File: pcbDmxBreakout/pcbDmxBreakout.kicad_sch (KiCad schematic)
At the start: 16 parts

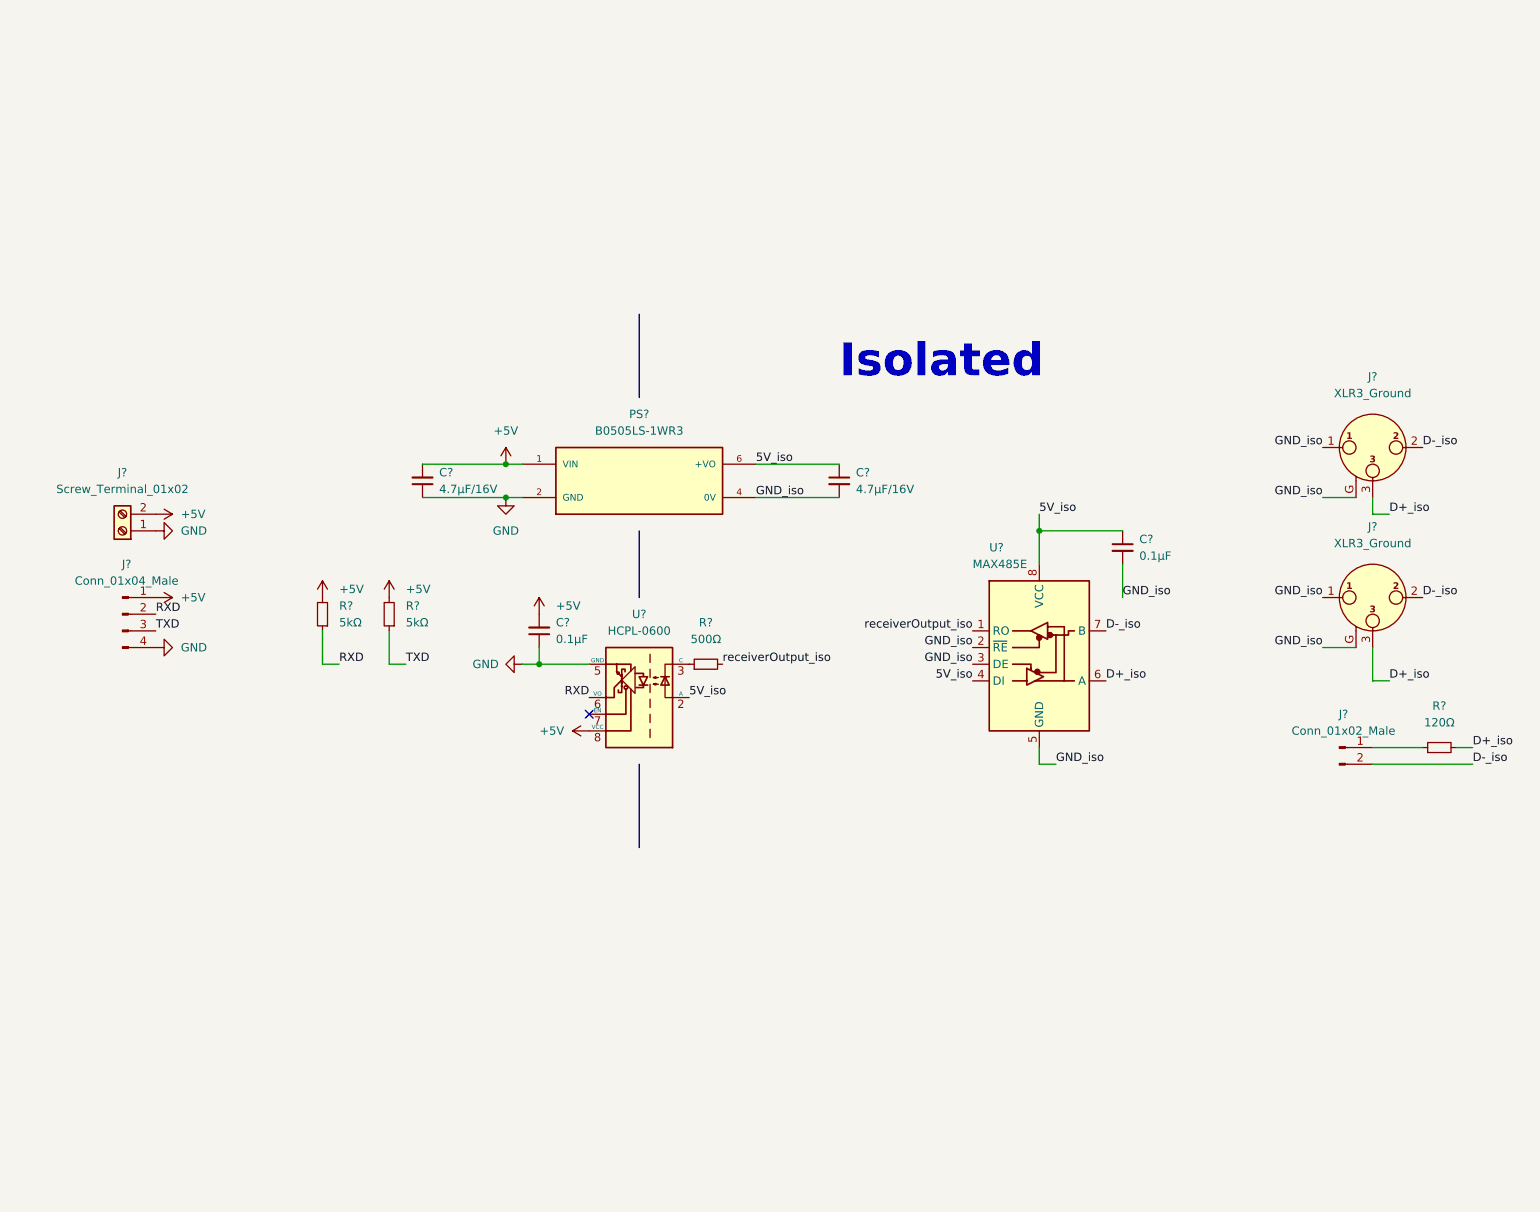
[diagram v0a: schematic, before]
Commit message: add Breakout board PCB
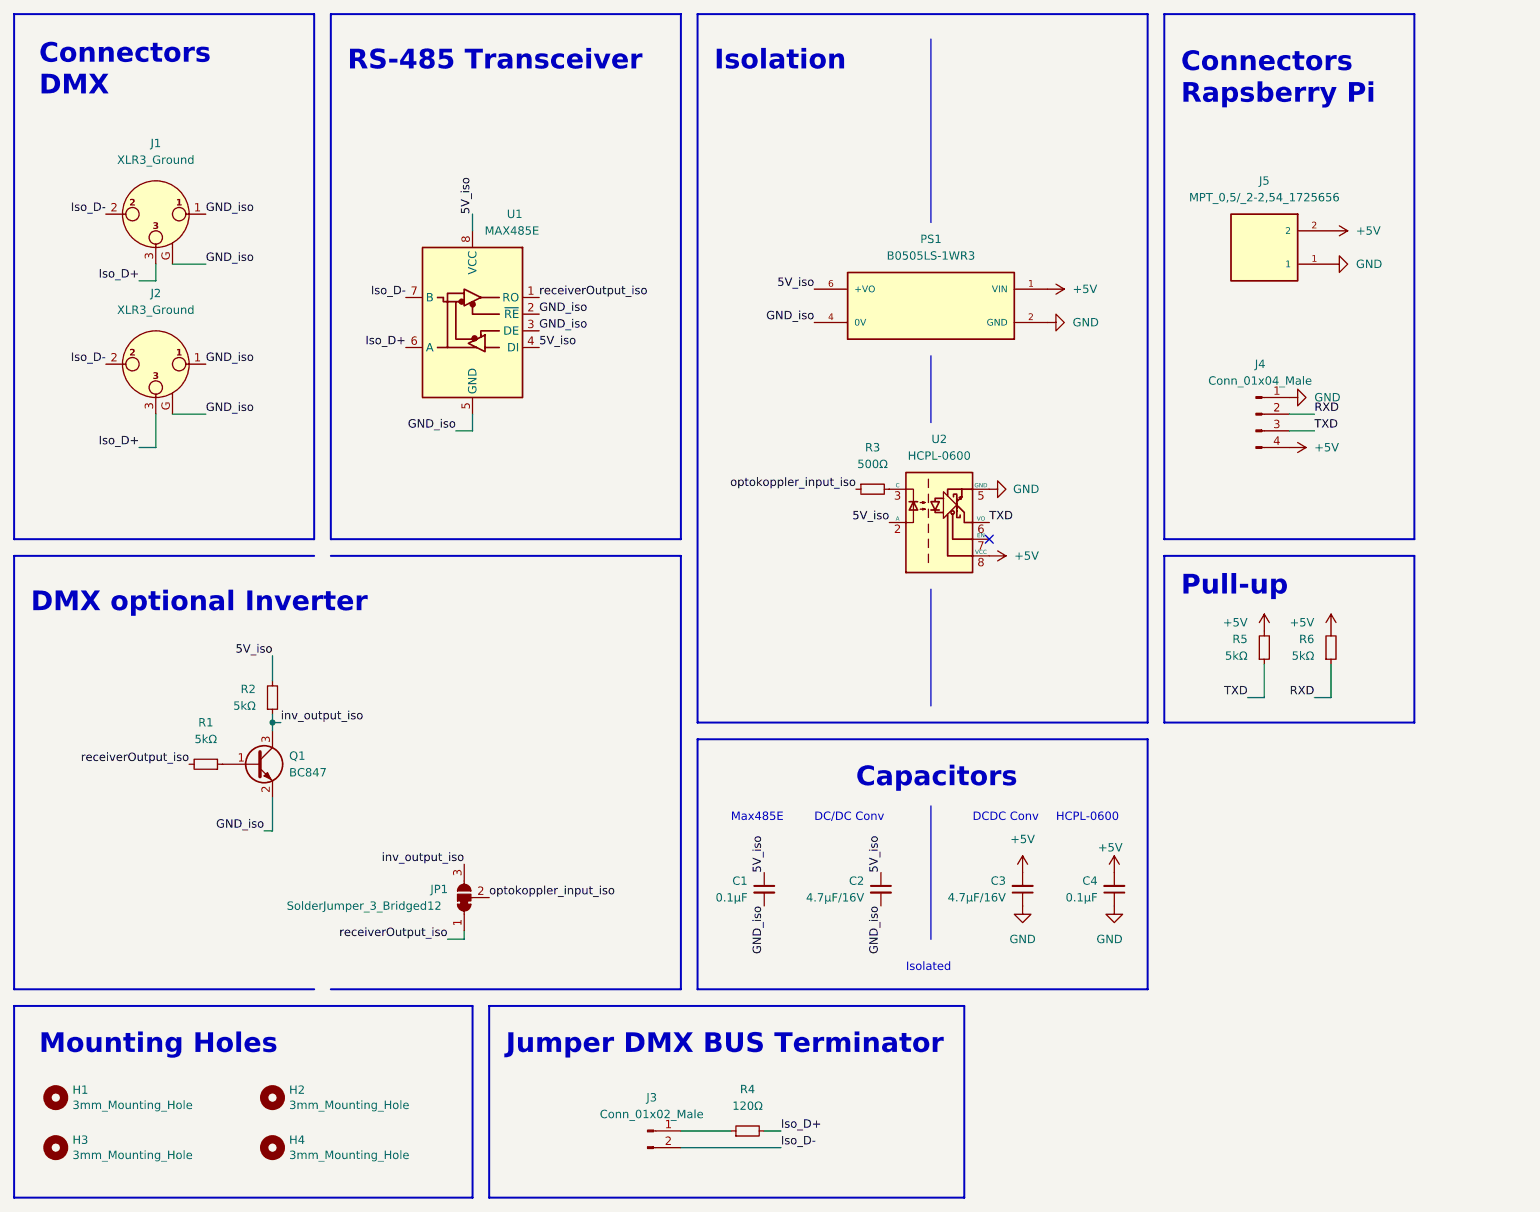
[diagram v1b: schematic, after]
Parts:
- removed J?: Screw_Terminal_01x02, symbol Connector:Screw_Terminal_01x02
- removed R?: 500Ω, symbol Device:R_Small
- added H1, H2, H3, H4: 3mm_Mounting_Hole, MountingHole:MountingHole_3mm, symbol Mechanical:MountingHole
- added J5: MPT_0,5/_2-2,54_1725656, local:PH_MPT_0,5__2-2,54_1725656, symbol Screw Terminal:MPT_0,5/_2-2,54_1725656
- added JP1: SolderJumper_3_Bridged12, Jumper:SolderJumper-3_P1.3mm_Bridged12_RoundedPad1.0x1.5mm_NumberLabels, symbol Jumper:SolderJumper_3_Bridged12
- added Q1: BC847, Package_TO_SOT_SMD:SOT-23, symbol Transistor_BJT:BC847
- added R1, R2: 5kΩ, Resistor_SMD:R_0805_2012Metric, symbol Device:R_Small
- added R3: 500Ω, Resistor_SMD:R_0805_2012Metric, symbol Device:R_Small
- C1, C4: renamed from C?; footprint (none) -> Capacitor_SMD:C_0805_2012Metric; mouser PartNr (none) -> 710-885012207045; mpn (none) -> 885012207045
- C2, C3: renamed from C?; footprint (none) -> Capacitor_SMD:C_0805_2012Metric; mouser PartNr (none) -> 187-CL21A475KQFNNNE; mpn (none) -> CL21A475KQFNNNE
- J1: renamed from J?; footprint (none) -> local:NEUTRIK_NC3MAH; mouser PartNr (none) -> 568-NC3MAH-LR; mpn (none) -> NC3MAH-LR
- J2: renamed from J?; footprint (none) -> local:NEUTRIK_NC3FAH2; mouser PartNr (none) -> 568-NC3FAH-2; mpn (none) -> NC3FAH2
- J3: renamed from J?; footprint (none) -> Connector_PinHeader_2.54mm:PinHeader_1x02_P2.54mm_Vertical; mouser PartNr (none) -> 649-67997-100HLF; mpn (none) -> 67997-100HLF
- J4: renamed from J?; footprint (none) -> Connector_PinHeader_2.54mm:PinHeader_1x04_P2.54mm_Horizontal; mouser PartNr (none) -> 649-67997-100HLF; mpn (none) -> 67997-100HLF
- PS1: renamed from PS?; footprint CONV_B0505LS-1WR3 -> local:CONV_B0505LS-1WR3; mouser PartNr (none) -> 919-RFB-0505S; mpn (none) -> RFB-0505S
- R4: renamed from R?; footprint (none) -> Resistor_SMD:R_0805_2012Metric; mouser PartNr (none) -> 755-SDR10EZPJ121; mpn (none) -> SDR10EZPJ121
- R5, R6: renamed from R?; footprint (none) -> Resistor_SMD:R_0805_2012Metric; mouser PartNr (none) -> 71-CRCW0805J-5K; mpn (none) -> CRCW08055K00JNTA
- U1: renamed from U?; footprint (none) -> Package_SO:SO-8_3.9x4.9mm_P1.27mm; mouser PartNr (none) -> 700-MAX485CSA; mpn (none) -> MAX485CSA+
- U2: renamed from U?; footprint Package_SO:SOIC-8_3.9x4.9mm_P1.27mm -> Package_SO:SO-8_3.9x4.9mm_P1.27mm; mouser PartNr (none) -> 630-HCPL-0600-560E; mpn (none) -> HCPL-0600-560E
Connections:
- net +5V: now also J4.4 (Pin_4), J5.2; no longer J4.1 (Pin_1)
- net 5V_iso: now also R2.2
- net GND: now also J4.1 (Pin_1), J5.1; no longer J4.4 (Pin_4)
- net GND_iso: now also Q1.2 (E)
- net RXD: no longer U2.6 (VO)
- net TXD: now also U2.6 (VO)
- net receiverOutput_iso: now also JP1.1 (A), R1.2
- net at U2.3 (C): now also R3.2
- net D+_iso renamed Iso_D+
- net D-_iso renamed Iso_D-
- new net: Q1.1 (B), R1.1
- new net inv_output_iso: JP1.3 (B), Q1.3 (C), R2.1
- new net optokoppler_input_iso: JP1.2 (C), R3.1
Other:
- note added: "Capacitors"
- note added: "Connectors DMX"
- note added: "Connectors Rapsberry Pi"
- note added: "DC/DC Conv"
- note added: "DCDC Conv"
- note added: "DMX optional Inverter"
- note added: "HCPL-0600"
- note added: "Isolation"
- note added: "Jumper DMX BUS Terminator"
- note added: "Max485E"
- note added: "Mounting Holes"
- note added: "Pull-up"
- note added: "RS-485 Transceiver"
- moved on the sheet: C1, C2, C3, C4, J1, J2, J3, J4, PS1, R4, R5, R6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
